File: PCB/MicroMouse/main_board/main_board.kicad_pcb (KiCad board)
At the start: 2 copper layers, 75 x 108.5 mm, 21 parts, among them J1 Conn_01x06, J2 Conn_01x06, J3 Conn_01x06, U2 LT8608, U3 TB6612FNG, U4 ESP32-WROOM-32U

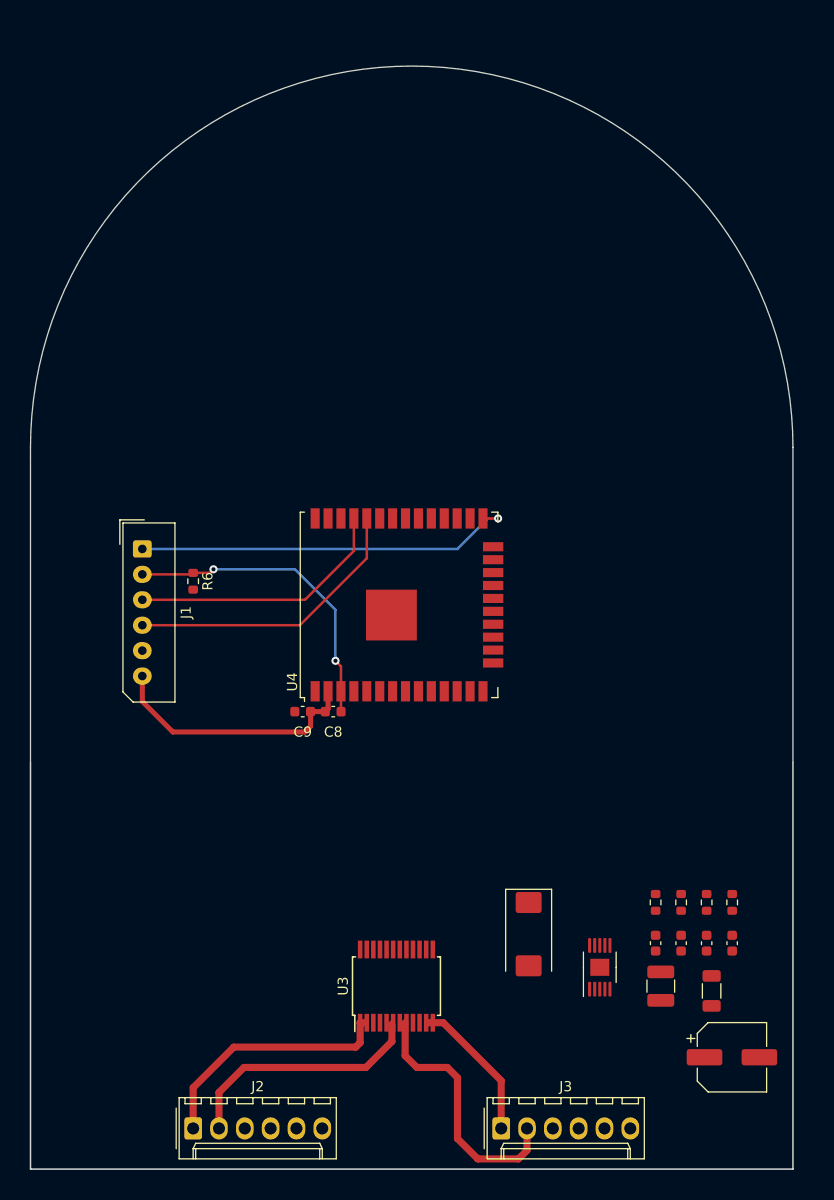
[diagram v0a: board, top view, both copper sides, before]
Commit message: atmel328p for reading ToF sensors
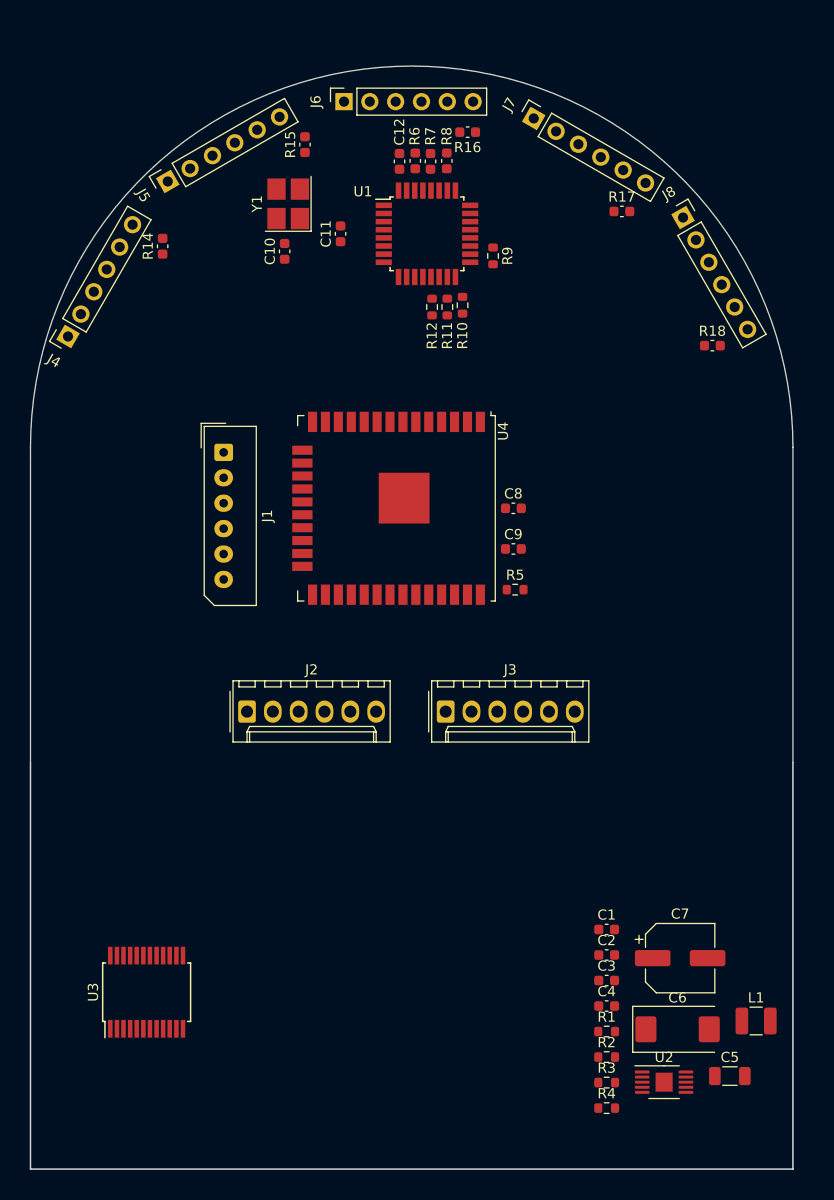
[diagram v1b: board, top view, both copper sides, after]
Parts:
- added C10: 22p, Capacitor_SMD:C_0603_1608Metric, F.Cu at (110.0, 69.7)
- added C11: 22p, Capacitor_SMD:C_0603_1608Metric, F.Cu at (115.5, 68.0)
- added C12: 100n, Capacitor_SMD:C_0603_1608Metric, F.Cu at (121.3, 60.9)
- added J4: Conn_01x06, Connector_PinSocket_2.54mm:PinSocket_1x06_P2.54mm_Vertical, F.Cu at (88.7, 78.1)
- added J5: Conn_01x06, Connector_PinSocket_2.54mm:PinSocket_1x06_P2.54mm_Vertical, F.Cu at (98.5, 62.9)
- added J6: Conn_01x06, Connector_PinSocket_2.54mm:PinSocket_1x06_P2.54mm_Vertical, F.Cu at (115.8, 55.0)
- added J7: Conn_01x06, Connector_PinSocket_2.54mm:PinSocket_1x06_P2.54mm_Vertical, F.Cu at (134.5, 56.6)
- added J8: Conn_01x06, Connector_PinSocket_2.54mm:PinSocket_1x06_P2.54mm_Vertical, F.Cu at (149.2, 66.4)
- added R10: 10k, Resistor_SMD:R_0603_1608Metric, F.Cu at (127.5, 75.0)
- added R11: 10k, Resistor_SMD:R_0603_1608Metric, F.Cu at (126.0, 75.2)
- added R12: 10k, Resistor_SMD:R_0603_1608Metric, F.Cu at (124.5, 75.2)
- added R14: 10k, Capacitor_SMD:C_0603_1608Metric, F.Cu at (98.0, 69.2)
- added R15: 10k, Capacitor_SMD:C_0603_1608Metric, F.Cu at (112.0, 59.2)
- added R16: 10k, Capacitor_SMD:C_0603_1608Metric, F.Cu at (128.0, 58.0)
- added R17: 10k, Capacitor_SMD:C_0603_1608Metric, F.Cu at (143.2, 65.8)
- added R18: 10k, Capacitor_SMD:C_0603_1608Metric, F.Cu at (152.1, 79.0)
- added R5: 10k, Resistor_SMD:R_0603_1608Metric, F.Cu at (132.7, 103.0)
- added R7: 10k, Capacitor_SMD:C_0603_1608Metric, F.Cu at (124.3, 60.9)
- added R8: 10k, Capacitor_SMD:C_0603_1608Metric, F.Cu at (126.0, 60.8)
- added R9: 10k, Resistor_SMD:R_0603_1608Metric, F.Cu at (130.5, 70.2)
- added U1: ATmega328P-A, Package_QFP:TQFP-32_7x7mm_P0.8mm, F.Cu at (124.0, 68.0)
- added Y1: Crystal_GND23_Small, Crystal:Crystal_SMD_TXC_7M-4Pin_3.2x2.5mm_HandSoldering, F.Cu at (110.3, 65.0)
- C8: value C -> 100n
- C9: value C -> 1u
- R6: value R -> 10k; footprint Resistor_SMD:R_0603_1608Metric -> Capacitor_SMD:C_0603_1608Metric
- moved R6 46.8 mm to (122.8, 60.8)
- moved J3 41.4 mm to (125.8, 115.0)
- moved J2 41.3 mm to (106.3, 115.0)
- moved C8 26.7 mm to (132.5, 95.0)
- moved C9 26.2 mm to (132.5, 99.0), turned to 0 degrees
- moved U3 24.6 mm to (96.4, 142.6)
- moved R4 23.7 mm to (141.7, 154.0), turned to 0 degrees
- moved R3 20.3 mm to (141.7, 151.5), turned to 0 degrees
- moved C6 17.4 mm to (148.7, 146.2), turned to 0 degrees
- moved R2 16.9 mm to (141.7, 149.0), turned to 0 degrees
- moved C4 13.8 mm to (141.7, 144.0), turned to 0 degrees
- moved R1 13.6 mm to (141.7, 146.5), turned to 0 degrees
- moved U2 12.9 mm to (147.3, 151.4), turned to 0 degrees
- moved J1 12.4 mm to (104.0, 89.5)
- moved C7 11.0 mm to (148.9, 139.2)
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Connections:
- R6 pad 1: RTS -> +3V3
- R6 pad 2: GND -> RESET_ATMEL
- U4 pad 29: IN2B -> SS_ATMEL
- U4 pad 30: unconnected-(U4-IO18-Pad30) -> SCK_ATMEL
- U4 pad 31: unconnected-(U4-IO19-Pad31) -> MISO_ATMEL
- U4 pad 36: unconnected-(U4-IO22-Pad36) -> RESET_ATMEL
- U4 pad 37: unconnected-(U4-IO23-Pad37) -> MOSI_ATMEL
- U4 pad 6: unconnected-(U4-IO34-Pad6) -> HALL_MOTORB_A
- U4 pad 7: unconnected-(U4-IO35-Pad7) -> HALL_MOTORB_B
- U4 pad 8: unconnected-(U4-IO32-Pad8) -> HALL_MOTORA_A
- U4 pad 9: unconnected-(U4-IO33-Pad9) -> HALL_MOTORA_B
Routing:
- net CTS: track 37.7 -> 0.00 mm, vias 1 -> 0
- net RTS: track 31.1 -> 0.00 mm, vias 2 -> 0
- net RXD: track 28.7 -> 0.00 mm
- net TXD: track 26.0 -> 0.00 mm
- net +3V3: track 25.5 -> 0.00 mm
- net MOTORB-: track 25.5 -> 0.00 mm
- net MOTORA+: track 24.8 -> 0.00 mm
- net MOTORA-: track 24.4 -> 0.00 mm
- net MOTORB+: track 14.3 -> 0.00 mm

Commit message: second PCB
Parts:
- removed C7: 100u, Capacitor_SMD:CP_Elec_6.3x7.7
- removed J2, J3: Conn_01x06, Connector_Molex:Molex_KK-254_AE-6410-06A_1x06_P2.54mm_Vertical
- removed U3: TB6612FNG, Package_SO:SSOP-24_5.3x8.2mm_P0.65mm
- added H1: MountingHole, MountingHole:MountingHole_2.7mm_M2.5_DIN965_Pad, F.Cu at (89.0, 156.0)
- added H2: MountingHole, MountingHole:MountingHole_2.7mm_M2.5_DIN965_Pad, F.Cu at (156.0, 156.0)
- added H3: MountingHole, MountingHole:MountingHole_2.7mm_M2.5_DIN965_Pad, F.Cu at (156.0, 86.0)
- added H4: MountingHole, MountingHole:MountingHole_2.7mm_M2.5_DIN965_Pad, F.Cu at (89.0, 86.0)
- J4, J5, J6, J7, J8: moved to B.Cu
- moved J4 66.9 mm to (155.5, 77.4), turned to 30 degrees
- moved C5 60.8 mm to (143.0, 91.0), turned to 180 degrees
- moved R18 60.6 mm to (91.5, 80.8), turned to 90 degrees
- moved L1 55.1 mm to (147.6, 91.0)
- moved J8 54.4 mm to (94.8, 67.4), turned to 150 degrees
- moved U2 53.1 mm to (149.0, 98.3), turned to -90 degrees
- moved R4 49.9 mm to (142.4, 104.1), turned to 90 degrees
- moved R1 48.9 mm to (143.5, 97.6)
- moved C2 48.7 mm to (151.5, 91.2), turned to 180 degrees
- moved R14 48.0 mm to (146.0, 69.0)
- moved R3 47.5 mm to (145.5, 104.2), turned to 90 degrees
- moved J5 47.2 mm to (145.7, 62.8), turned to 60 degrees
- moved R2 45.3 mm to (148.5, 104.2), turned to 90 degrees
- moved R17 41.5 mm to (101.7, 65.5)
- moved C1 40.5 mm to (143.5, 96.0), turned to 180 degrees
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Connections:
- C4 pad 2: +6V -> +3V3
- C5 pad 1: +6V -> +3V3
- L1 pad 1: +6V -> +3V3
- R2 pad 1: +6V -> +3V3
- R4 pad 1: +6V -> +3V3
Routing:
- net +3V3: track 0.00 -> 38.2 mm
- net VCC: track 0.00 -> 24.0 mm
- net RTS: track 0.00 -> 15.4 mm
- net Net-(U2-RT): track 0.00 -> 7.71 mm
- net Net-(U2-FB): track 0.00 -> 7.52 mm
- net Net-(U2-SW): track 0.00 -> 7.26 mm
- net Net-(U2-INTVCC): track 0.00 -> 7.22 mm
- net Net-(U2-BST): track 0.00 -> 5.90 mm
- net Net-(U2-TR/SS): track 0.00 -> 3.81 mm
- net Net-(U2-PG): track 0.00 -> 3.06 mm
- added copper zone on B.Cu, net GND
- added copper zone on F.Cu, net GND

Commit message: PCB prototype
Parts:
- removed C10, C11: 22p, Capacitor_SMD:C_0603_1608Metric
- removed C12: 100n, Capacitor_SMD:C_0603_1608Metric
- removed R10, R11, R12, R9: 10k, Resistor_SMD:R_0603_1608Metric
- removed R6: 10k, Capacitor_SMD:C_0603_1608Metric
- removed Y1: Crystal_GND23_Small, Crystal:Crystal_SMD_TXC_7M-4Pin_3.2x2.5mm_HandSoldering
- added J10: Conn_01x05, Connector_PinSocket_2.54mm:PinSocket_1x05_P2.54mm_Vertical, F.Cu at (147.7, 81.5)
- added J11: Conn_01x02, Connector_PinSocket_2.54mm:PinSocket_1x02_P2.54mm_Vertical, F.Cu at (92.0, 123.0)
- added J12: Conn_01x04, Connector_PinSocket_1.27mm:PinSocket_1x04_P1.27mm_Vertical, F.Cu at (91.5, 102.2)
- added J2: Conn_01x02, Connector_PinSocket_2.54mm:PinSocket_1x02_P2.54mm_Vertical, F.Cu at (150.5, 122.8)
- added J3: Conn_01x04, Connector_PinSocket_1.27mm:PinSocket_1x04_P1.27mm_Vertical, F.Cu at (157.0, 102.2)
- added J9: Conn_01x02, Connector_PinSocket_2.54mm:PinSocket_1x02_P2.54mm_Vertical, F.Cu at (131.5, 113.8)
- added U3: TB6612FNG, Package_SO:SSOP-24_5.3x8.2mm_P0.65mm, F.Cu at (116.5, 108.5)
- U1: value ATmega328P-A -> PCF8574; footprint Package_QFP:TQFP-32_7x7mm_P0.8mm -> Package_SO:SOIC-16W_7.5x10.3mm_P1.27mm
- moved R18 26.7 mm to (116.5, 71.3)
- moved R14 24.5 mm to (123.5, 59.2), turned to -90 degrees
- moved R17 18.4 mm to (119.0, 59.2), turned to -90 degrees
- moved R7 18.4 mm to (113.9, 76.0), turned to 0 degrees
- moved R8 16.7 mm to (118.9, 76.0), turned to 180 degrees
- moved R15 12.1 mm to (122.0, 59.2), turned to -90 degrees
- moved C8 8.05 mm to (114.4, 98.8)
- moved C9 8.05 mm to (111.4, 98.8)
- moved J1 8.05 mm to (105.2, 94.0)
- moved R5 8.05 mm to (108.9, 92.5)
- moved U4 8.05 mm to (120.0, 87.5)
- moved R16 6.04 mm to (120.5, 59.2), turned to -90 degrees
- moved C1 4.47 mm to (141.5, 100.0)
- moved C2 4.47 mm to (149.5, 95.2)
- moved C3 4.47 mm to (145.0, 108.2)
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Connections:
- C4 pad 2: +3V3 -> 3v3
- C5 pad 1: +3V3 -> 3v3
- C8 pad 1: +3V3 -> 3v3
- C9 pad 1: +3V3 -> 3v3
- J1 pad 6: +3V3 -> 3v3
- J4 pad 1: +3V3 -> 3v3
- J5 pad 1: +3V3 -> 3v3
- J6 pad 1: +3V3 -> 3v3
- J7 pad 1: +3V3 -> 3v3
- J8 pad 1: +3V3 -> 3v3
- L1 pad 1: +3V3 -> 3v3
- R14 pad 1: +3V3 -> 3v3
- R15 pad 1: +3V3 -> 3v3
- R16 pad 1: +3V3 -> 3v3
- R17 pad 1: +3V3 -> 3v3
- R18 pad 1: +3V3 -> 3v3
- R2 pad 1: +3V3 -> 3v3
- R4 pad 1: +3V3 -> 3v3
- R7 pad 1: +3V3 -> 3v3
- R8 pad 1: +3V3 -> 3v3
- U1 pad 1: XSHUT2 -> GND
- U1 pad 10: XSHUT5 -> unconnected-(U1-P5-Pad10)
- U1 pad 14: SS_ATMEL -> SCL
- U1 pad 15: MOSI_ATMEL -> SDA
- U1 pad 16: MISO_ATMEL -> 3v3
- U1 pad 2: XSHUT3 -> GND
- U1 pad 4: +3V3 -> XSHUT1
- U1 pad 5: GND -> XSHUT2
- U1 pad 6: +3V3 -> XSHUT3
- U1 pad 7: unconnected-(U1-XTAL1/PB6-Pad7) -> XSHUT4
- U1 pad 8: unconnected-(U1-XTAL2/PB7-Pad8) -> GND
- U1 pad 9: XSHUT4 -> XSHUT5
- U4 pad 10: PWMA -> unconnected-(U4-IO25-Pad10)
- U4 pad 11: IN1B -> unconnected-(U4-IO26-Pad11)
- U4 pad 12: IN1A -> unconnected-(U4-IO27-Pad12)
- U4 pad 14: IN2A -> unconnected-(U4-IO12-Pad14)
- U4 pad 16: PWMB -> unconnected-(U4-IO13-Pad16)
- U4 pad 2: +3V3 -> 3v3
- U4 pad 24: unconnected-(U4-IO2-Pad24) -> PWMB
- U4 pad 26: unconnected-(U4-IO4-Pad26) -> IN2B
- U4 pad 27: unconnected-(U4-IO16-Pad27) -> IN2A
- U4 pad 28: unconnected-(U4-IO17-Pad28) -> PWMA
- U4 pad 29: SS_ATMEL -> unconnected-(U4-IO5-Pad29)
- U4 pad 30: SCK_ATMEL -> IN1B
- U4 pad 31: MISO_ATMEL -> IN1A
- U4 pad 33: unconnected-(U4-IO21-Pad33) -> SDA
- U4 pad 36: RESET_ATMEL -> SCL
- U4 pad 37: MOSI_ATMEL -> unconnected-(U4-IO23-Pad37)
- U4 pad 6: HALL_MOTORB_A -> HALL_MOTORA_A
- U4 pad 7: HALL_MOTORB_B -> HALL_MOTORA_B
- U4 pad 8: HALL_MOTORA_A -> HALL_MOTORB_B
- U4 pad 9: HALL_MOTORA_B -> HALL_MOTORB_A
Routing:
- net 3v3: track 0.00 -> 325.7 mm, vias 0 -> 7
- net SDA: track 0.00 -> 148.0 mm, vias 0 -> 4
- net SCL: track 0.00 -> 141.2 mm, vias 0 -> 1
- net IN1A: track 0.00 -> 72.1 mm, vias 0 -> 4
- net IN1B: track 0.00 -> 69.9 mm, vias 0 -> 4
- net PWMA: track 0.00 -> 68.2 mm, vias 0 -> 4
- net IN2A: track 0.00 -> 60.5 mm, vias 0 -> 2
- net IN2B: track 0.00 -> 51.0 mm, vias 0 -> 2
- net HALL_MOTORB_B: track 0.00 -> 43.8 mm, vias 0 -> 1
- net HALL_MOTORB_A: track 0.00 -> 43.0 mm, vias 0 -> 1
- net MOTORB-: track 0.00 -> 42.5 mm
- net PWMB: track 0.00 -> 40.4 mm, vias 0 -> 2
- net +3V3: track 38.2 -> 0.00 mm
- net CTS: track 0.00 -> 38.2 mm, vias 0 -> 1
- net MOTORB+: track 0.00 -> 37.8 mm
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
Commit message: lost changes from old PC
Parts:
- moved J2 27.2 mm to (123.5, 119.3), turned to -90 degrees
- moved J11 20.9 mm to (112.5, 119.2), turned to 90 degrees
- moved J3 7.75 mm to (149.2, 102.2)
- moved J12 4.25 mm to (95.8, 102.2)
- moved C2 3.96 mm to (146.2, 97.4)
- moved C6 3.44 mm to (133.2, 113.4)
- moved J9 3.44 mm to (128.3, 112.6)
- moved C3 2.05 mm to (142.9, 107.9)
- moved R1 2.05 mm to (139.5, 101.3)
- moved C1 2.05 mm to (139.5, 99.7)
- moved C4 2.05 mm to (139.9, 107.9)
- moved C5 2.05 mm to (138.9, 94.7)
- moved L1 2.05 mm to (143.6, 94.7)
- moved R2 2.05 mm to (144.5, 107.9)
- moved R3 2.05 mm to (141.4, 107.9)
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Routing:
- net MOTORB-: track 42.5 -> 9.05 mm
- net MOTORB+: track 37.8 -> 9.40 mm
- net MOTORA-: track 33.1 -> 7.88 mm
- net MOTORA+: track 27.4 -> 7.76 mm
- net 3v3: track 325.7 -> 315.3 mm
- net HALL_MOTORB_B: track 43.8 -> 36.4 mm
- net HALL_MOTORB_A: track 43.0 -> 35.7 mm
- net HALL_MOTORA_A: track 30.5 -> 26.3 mm
- net HALL_MOTORA_B: track 33.1 -> 28.9 mm
- net IN2A: track 60.5 -> 57.0 mm
- net Net-(U2-BST): track 5.90 -> 2.95 mm
- net CTS: track 38.2 -> 36.3 mm
- net GND: track 2.17 -> 3.14 mm, vias 10 -> 12
- net VCC: track 29.5 -> 28.6 mm
- net Net-(U2-SW): track 7.26 -> 6.47 mm

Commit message: ready for manufacture
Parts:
- added H10: MountingHole, MountingHole:MountingHole_2.7mm_M2.5_DIN965_Pad, F.Cu at (156.0, 126.0)
- added H11: MountingHole, MountingHole:MountingHole_2.7mm_M2.5_DIN965_Pad, F.Cu at (89.0, 136.0)
- added H12: MountingHole, MountingHole:MountingHole_2.7mm_M2.5_DIN965_Pad, F.Cu at (89.0, 116.0)
- added H13: MountingHole, MountingHole:MountingHole_2.7mm_M2.5_DIN965_Pad, F.Cu at (156.0, 136.0)
- added H14: MountingHole, MountingHole:MountingHole_2.7mm_M2.5_DIN965_Pad, F.Cu at (89.0, 146.0)
- added H15: MountingHole, MountingHole:MountingHole_2.7mm_M2.5_DIN965_Pad, F.Cu at (89.0, 126.0)
- added H16: MountingHole, MountingHole:MountingHole_2.7mm_M2.5_DIN965_Pad, F.Cu at (156.0, 146.0)
- added H17: MountingHole, MountingHole:MountingHole_2.7mm_M2.5_DIN965_Pad, F.Cu at (104.0, 116.0)
- added H18: MountingHole, MountingHole:MountingHole_2.7mm_M2.5_DIN965_Pad, F.Cu at (141.0, 116.0)
- added H19: MountingHole, MountingHole:MountingHole_2.7mm_M2.5_DIN965_Pad, F.Cu at (119.0, 122.0)
- added H20: MountingHole, MountingHole:MountingHole_2.7mm_M2.5_DIN965_Pad, F.Cu at (126.0, 122.0)
- added H5: MountingHole, MountingHole:MountingHole_2.7mm_M2.5_DIN965_Pad, F.Cu at (156.0, 96.0)
- added H6: MountingHole, MountingHole:MountingHole_2.7mm_M2.5_DIN965_Pad, F.Cu at (156.0, 106.0)
- added H7: MountingHole, MountingHole:MountingHole_2.7mm_M2.5_DIN965_Pad, F.Cu at (156.0, 116.0)
- added H8: MountingHole, MountingHole:MountingHole_2.7mm_M2.5_DIN965_Pad, F.Cu at (89.0, 106.0)
- added H9: MountingHole, MountingHole:MountingHole_2.7mm_M2.5_DIN965_Pad, F.Cu at (89.0, 96.0)
- moved J2 2.28 mm to (123.5, 117.0)
- moved J11 2.17 mm to (112.5, 117.0)
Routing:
- net VCC: track 28.6 -> 35.3 mm
- net SDA: track 148.0 -> 145.0 mm, vias 4 -> 6
- net MOTORB+: track 9.40 -> 7.12 mm
- net MOTORA-: track 7.88 -> 5.70 mm
- net MOTORA+: track 7.76 -> 5.58 mm
- net MOTORB-: track 9.05 -> 7.01 mm
- net GND: track 3.14 -> 3.51 mm, vias 12 -> 230

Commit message: some changes on PCB after consultations with Mr. micromouse FEI
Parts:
- removed J6: Conn_01x06, Connector_PinSocket_2.54mm:PinSocket_1x06_P2.54mm_Vertical
- removed R16: 10k, Capacitor_SMD:C_0603_1608Metric
- removed U1: PCF8574, Package_SO:SOIC-16W_7.5x10.3mm_P1.27mm
- J4, J5, J7, J8: moved to F.Cu
- moved J4 63.5 mm to (92.0, 78.0), turned to 100 degrees
- moved J8 46.4 mm to (140.5, 75.8), turned to 80 degrees
- moved R15 36.5 mm to (151.7, 80.4), turned to -10 degrees
- moved J5 26.5 mm to (120.0, 56.1), turned to -45 degrees
- moved R17 20.8 mm to (103.8, 73.4), turned to 10 degrees
- moved R18 15.7 mm to (131.5, 66.5), turned to 135 degrees
- moved J7 15.4 mm to (125.0, 56.1), turned to 45 degrees
- moved R14 12.4 mm to (113.5, 66.5), turned to -135 degrees
- moved J10 2.61 mm to (147.8, 84.1)
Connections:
- R14 pad 2: XSHUT1 -> XSHUT2
- R15 pad 2: XSHUT2 -> XSHUT5
- R17 pad 2: XSHUT4 -> XSHUT1
- R18 pad 1: 3v3 -> XSHUT4
- R18 pad 2: XSHUT5 -> 3v3
- U4 pad 10: unconnected-(U4-IO25-Pad10) -> XSHUT4
- U4 pad 14: unconnected-(U4-IO12-Pad14) -> XSHUT5
- U4 pad 29: unconnected-(U4-IO5-Pad29) -> XSHUT2
- U4 pad 37: unconnected-(U4-IO23-Pad37) -> XSHUT1
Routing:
- net SDA: track 145.0 -> 103.3 mm, vias 6 -> 0
- net SCL: track 141.2 -> 101.9 mm, vias 1 -> 0
- net 3v3: track 315.0 -> 278.4 mm, vias 7 -> 10
- net IN1B: track 69.9 -> 42.8 mm, vias 4 -> 2
- net PWMA: track 68.2 -> 41.2 mm, vias 4 -> 2
- net IN1A: track 72.1 -> 46.9 mm, vias 4 -> 2
- net XSHUT3: track 23.7 -> 0.00 mm, vias 1 -> 0
- net XSHUT1: track 33.5 -> 16.2 mm, vias 0 -> 2
- net XSHUT5: track 34.9 -> 45.0 mm, vias 0 -> 2
- net XSHUT2: track 29.1 -> 20.5 mm, vias 2 -> 0
- net XSHUT4: track 28.0 -> 35.6 mm
- net CTS: track 36.3 -> 34.5 mm
- net HALL_MOTORA_A: track 26.3 -> 27.4 mm
- net GND: vias 230 -> 149
